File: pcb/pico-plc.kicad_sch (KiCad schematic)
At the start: 9 parts, among them SW1 Reset, SW2 Power Cycle

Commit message: Use larger screw terminals, adjust layout to suit
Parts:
- removed SW1: Reset, Button_Switch_SMD:SW_Push_1P1T_NO_CK_KMR2, symbol Switch:SW_Push
- removed SW2: Power Cycle, Button_Switch_SMD:SW_Push_1P1T_NO_CK_KMR2, symbol Switch:SW_Push
- H1, H2, H3, H4: footprint MountingHole:MountingHole_3.2mm_M3 -> MountingHole:MountingHole_3.2mm_M3_Pad_Via; symbol Mechanical:MountingHole -> Mechanical:MountingHole_Pad
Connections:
- net GND: now also H1.1, H2.1
- no-connect marks 1 -> 3

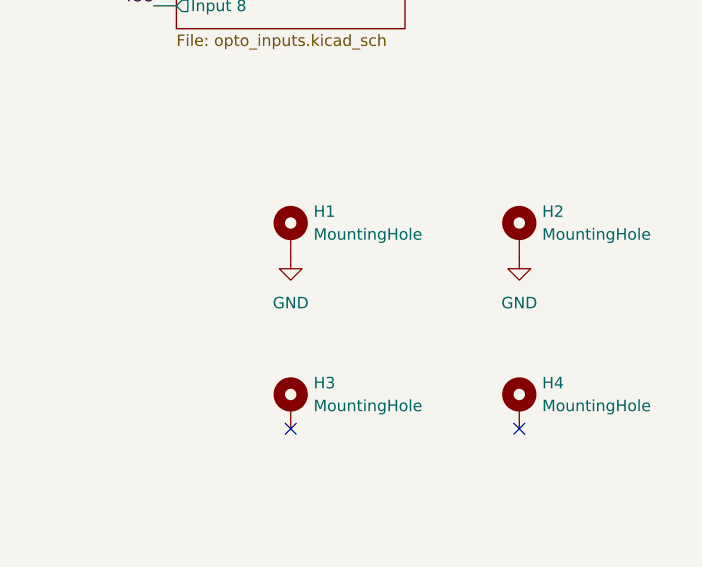
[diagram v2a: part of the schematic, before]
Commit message: pcb: disconnect mounting holes from GND, fix dimension annotations
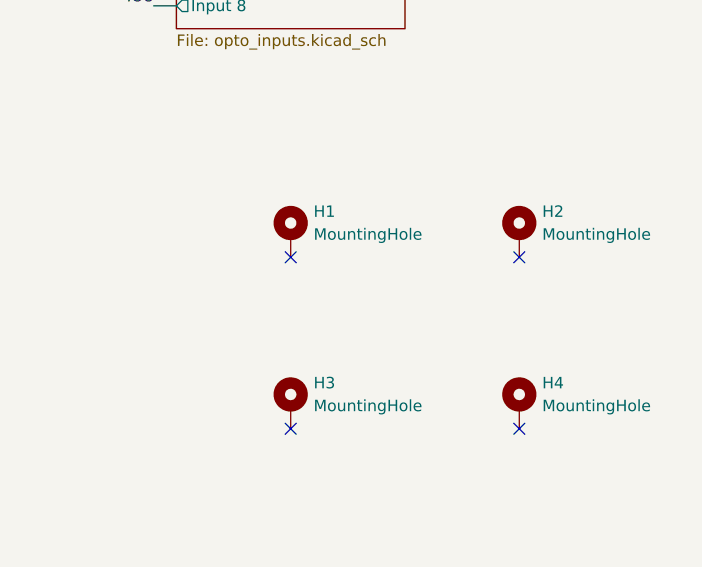
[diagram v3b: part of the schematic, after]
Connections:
- net GND: no longer H1.1, H2.1
- no-connect marks 3 -> 5
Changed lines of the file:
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@@
+	)
+	(no_connect
+		(at 228.6 137.16)
+	)
+	(no_connect
+		(at 254 137.16)
 	)
 	(no_connect
@@
 	)
 	(symbol
-		(lib_id "power:GND")
-		(at 254 137.16 0)
-		(unit 1)
-		(exclude_from_sim no)
-		(in_bom yes)
-		(on_board yes)
-		(dnp no)
-		(fields_autoplaced yes)
-		(property "Reference" "#PWR011"
-			(at 254 143.51 0)
-			(effects
-				(font
-					(size 1.27 1.27)
-				)
-				(hide yes)
-			)
-		)
-		(property "Value" "GND"
-			(at 254 142.24 0)
-			(effects
-				(font
-					(size 1.27 1.27)
-				)
-			)
-		)
-		(property "Footprint" ""
-			(at 254 137.16 0)
-			(effects
-				(font
-					(size 1.27 1.27)
-				)
-				(hide yes)
-			)
-		)
-		(property "Datasheet" ""
-			(at 254 137.16 0)
-			(effects
-				(font
-					(size 1.27 1.27)
-				)
-				(hide yes)
-			)
-		)
-		(property "Description" "Power symbol creates a global label with name \"GND\" , ground"
-			(at 254 137.16 0)
-			(effects
-				(font
-					(size 1.27 1.27)
-				)
-				(hide yes)
-			)
-		)
-		(pin "1"
-		)
-		(instances
-			(project "pico-plc"
-				(path "/fc9ff52a-d720-4efe-8661-3db6c88a54e4"
-					(reference "#PWR011")
-					(unit 1)
-				)
-			)
-		)
-	)
-	(symbol
 		(lib_id "Connector:TestPoint")
 		(at 76.2 165.1 90)
@@
 					(unit 1)
 				)
-			)
-		)
-	)
-	(symbol
-		(lib_id "power:GND")
-		(at 228.6 137.16 0)
-		(unit 1)
-		(exclude_from_sim no)
-		(in_bom yes)
-		(on_board yes)
-		(dnp no)
-		(fields_autoplaced yes)
-		(property "Reference" "#PWR014"
-			(at 228.6 143.51 0)
-			(effects
-				(font
-					(size 1.27 1.27)
-				)
-				(hide yes)
-			)
-		)
-		(property "Value" "GND"
-			(at 228.6 142.24 0)
-			(effects
-				(font
-					(size 1.27 1.27)
-				)
-			)
-		)
-		(property "Footprint" ""
-			(at 228.6 137.16 0)
-			(effects
-				(font
-					(size 1.27 1.27)
-				)
-				(hide yes)
-			)
-		)
-		(property "Datasheet" ""
-			(at 228.6 137.16 0)
-			(effects
-				(font
-					(size 1.27 1.27)
-				)
-				(hide yes)
-			)
-		)
-		(property "Description" "Power symbol creates a global label with name \"GND\" , ground"
-			(at 228.6 137.16 0)
-			(effects
-				(font
-					(size 1.27 1.27)
-				)
-				(hide yes)
-			)
-		)
-		(pin "1"
-		)
-		(instances
-			(project "pico-plc"
-				(path "/fc9ff52a-d720-4efe-8661-3db6c88a54e4"
-					(reference "#PWR014")
-					(unit 1)
-				)

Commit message: New board revision
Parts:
- removed TP1: Run, TestPoint:TestPoint_Pad_D2.0mm, symbol Connector:TestPoint
- removed TP2: 3.3V En, TestPoint:TestPoint_Pad_D2.0mm, symbol Connector:TestPoint
- added J1: Conn_01x09, Connector_PinHeader_2.54mm:PinHeader_1x09_P2.54mm_Vertical, symbol Connector_Generic:Conn_01x09
- A1: footprint RaspberryPi_Pico:RaspberryPi_Pico_Common -> Module:RaspberryPi_Pico_Common_THT; symbol RaspberryPi_Pico:RaspberryPi_Pico -> MCU_Module:RaspberryPi_Pico
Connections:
- net +3V3: now also J1.2 (Pin_2)
- net GND: now also J1.1 (Pin_1)
- net IO16: now also J1.9 (Pin_9)
- net IO17: now also J1.8 (Pin_8)
- net IO18: now also J1.7 (Pin_7)
- net IO19: now also J1.6 (Pin_6)
- net IO20: now also J1.5 (Pin_5)
- net IO21: now also J1.4 (Pin_4)
- net IO22: now also J1.3 (Pin_3)
- net 3V3_EN: no longer names the net of A1.37 (3V3_EN)
- net ADC_VREF: no longer names the net of A1.35 (ADC_VREF)
- net GNDA: no longer names the net of A1.33 (AGND)
- net IO26: no longer names the net of A1.31 (GPIO26_ADC0)
- net IO27: no longer names the net of A1.32 (GPIO27_ADC1)
- net RUN: no longer names the net of A1.30 (RUN)
- no-connect marks 5 -> 11
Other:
- removed sheet General IO
- note added: "IO 16-22 unusable on WIZnet EVB boards"
- moved on the sheet: A1
